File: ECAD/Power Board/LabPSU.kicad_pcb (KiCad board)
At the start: 2 copper layers, 83 parts, among them J1 CTRL, J2 DC-IN, J3 UPDI, J4 +, J5 -, Q1 Si7148DP, Q2 Si7148DP, U1 LM1117-3.3, U2 LM2594HVN-5.0, U3 LM5118MH, U4 TXB0104D, U5 LM358, U6 ATtiny414-SS, U7 INA180A3, U8 MCP4811

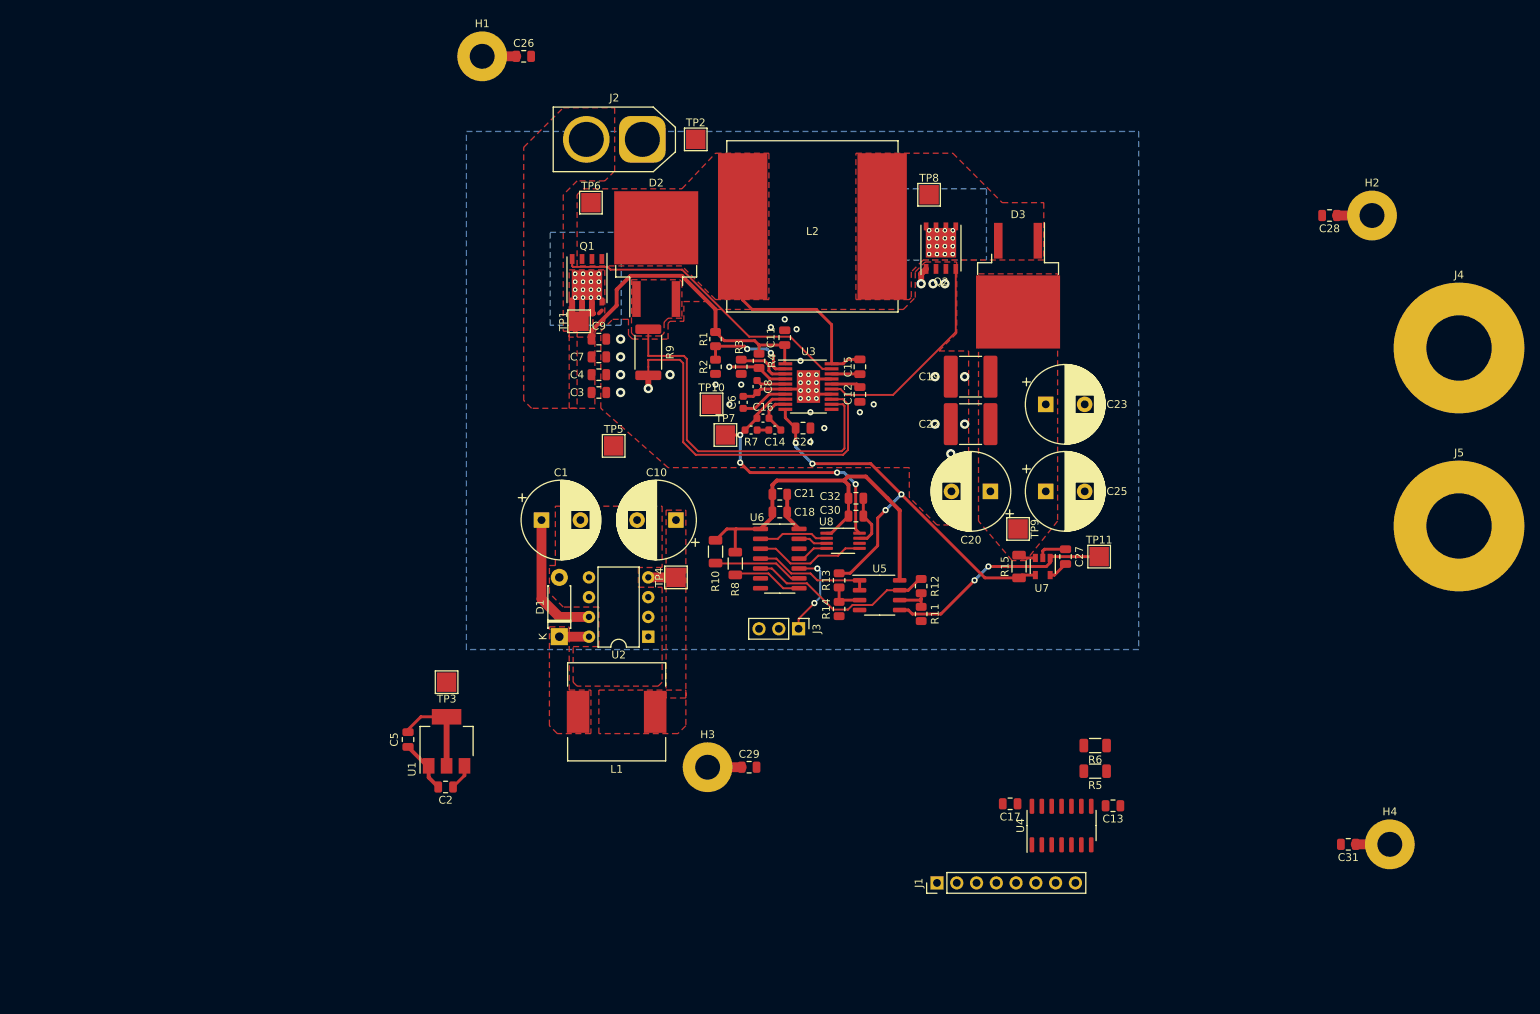
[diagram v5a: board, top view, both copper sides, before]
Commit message: Simplify the power board, remove level shifter
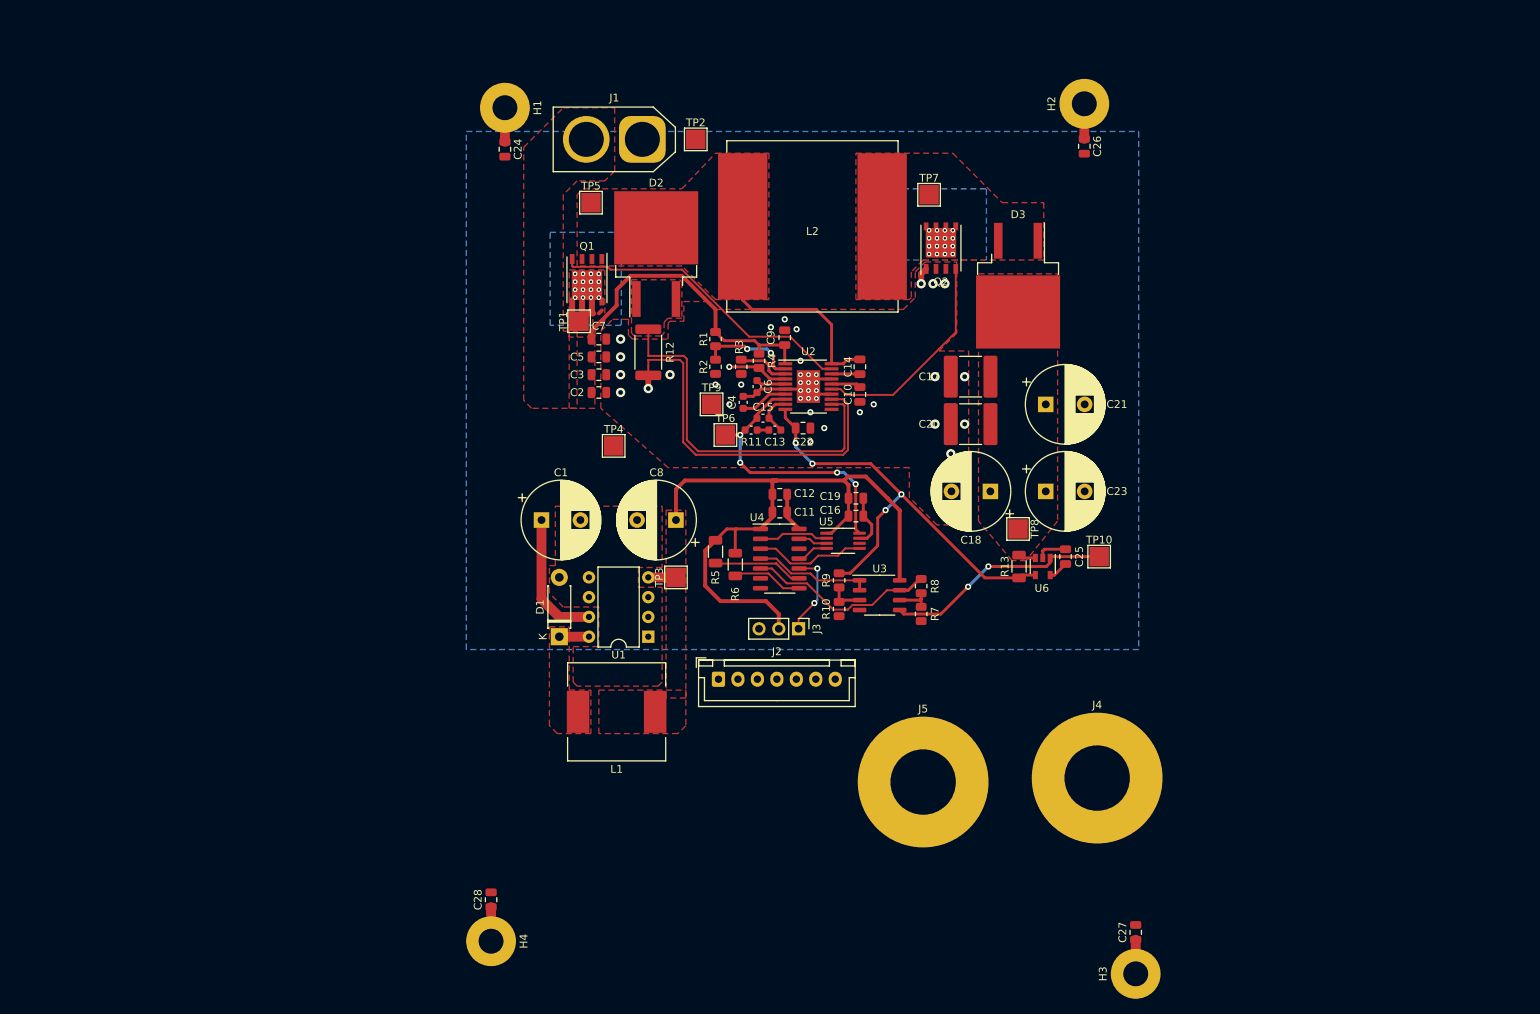
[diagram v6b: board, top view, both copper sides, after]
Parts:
- removed the C13 at (136.4, 146.8)
- removed the C17 at (123.2, 146.6)
- removed the C2 at (50.7, 144.4)
- removed the C5 at (45.8, 138.3)
- removed the J1 at (113.8, 156.7)
- removed the R5 at (134.1, 142.4)
- removed the R6 at (134.1, 139.1)
- removed the TP3 at (50.8, 130.9)
- removed the U1 at (50.8, 138.5)
- removed the U4 at (129.8, 149.4)
- added J2: CTRL, Connector_JST:JST_XH_B7B-XH-A_1x07_P2.50mm_Vertical, F.Cu at (85.7, 130.6)
- moved H4 116.1 mm to (56.5, 164.2), turned to 270 degrees
- moved C28 110.3 mm to (56.5, 158.9), turned to 90 degrees
- moved J5 76.3 mm to (112.0, 143.8)
- moved J4 72.2 mm to (134.4, 143.3)
- moved H3 61.1 mm to (139.3, 168.4), turned to 90 degrees
- moved C27 54.0 mm to (139.3, 163.1), turned to 90 degrees
- moved H2 39.6 mm to (132.7, 56.6), turned to 90 degrees
- moved C26 32.7 mm to (132.7, 62.1), turned to 270 degrees
- moved C24 12.2 mm to (58.3, 62.5), turned to 270 degrees
- moved H1 7.22 mm to (58.3, 57.1), turned to 270 degrees
- moved R6 3.03 mm to (87.9, 115.8)
- moved R5 2.96 mm to (85.3, 114.2)
- renumbered C12 to C10, C18 to C11, C21 to C12, C14 to C13, C15 to C14, C16 to C15, C30 to C16, C19 to C17, C20 to C18, C32 to C19, C3 to C2, C22 to C20, C23 to C21, C24 to C22, C25 to C23, C26 to C24, C27 to C25, C28 to C26, C29 to C27, C31 to C28, C4 to C3, C6 to C4, C7 to C5, C8 to C6, C9 to C7, C10 to C8, C11 to C9, J2 to J1, R14 to R10, R7 to R11, R9 to R12, R15 to R13, R8 to R5, R10 to R6, R11 to R7, R12 to R8, R13 to R9, TP11 to TP10, TP4 to TP3, TP5 to TP4, TP6 to TP5, TP7 to TP6, TP8 to TP7, TP9 to TP8, TP10 to TP9, U2 to U1, U3 to U2, U5 to U3, U6 to U4, U8 to U5, U7 to U6
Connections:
- R5 pad 2: SDA -> SCL
- R6 pad 2: SCL -> SDA
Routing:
- net +5V: track 61.4 -> 95.1 mm
- net +3V3: track 12.3 -> 0.00 mm
- net GND: track 43.6 -> 36.7 mm

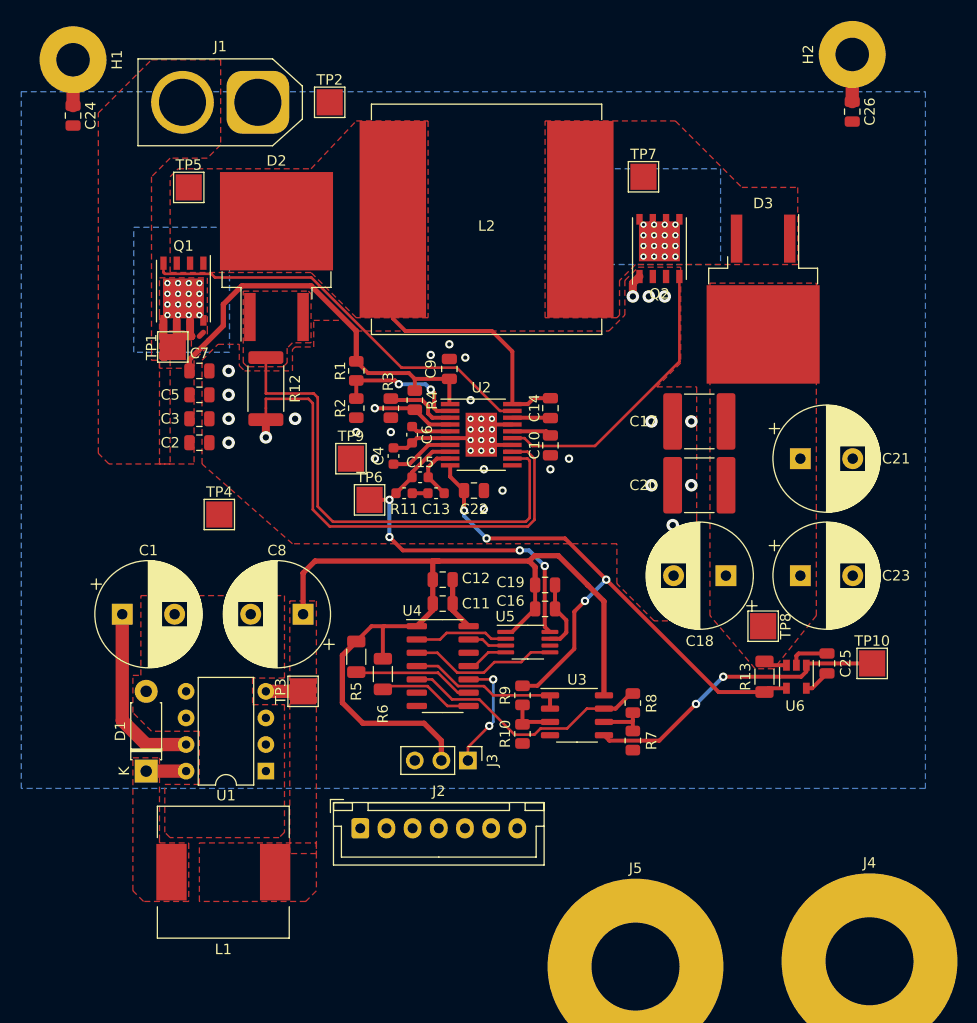
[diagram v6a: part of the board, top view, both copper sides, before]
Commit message: Place header
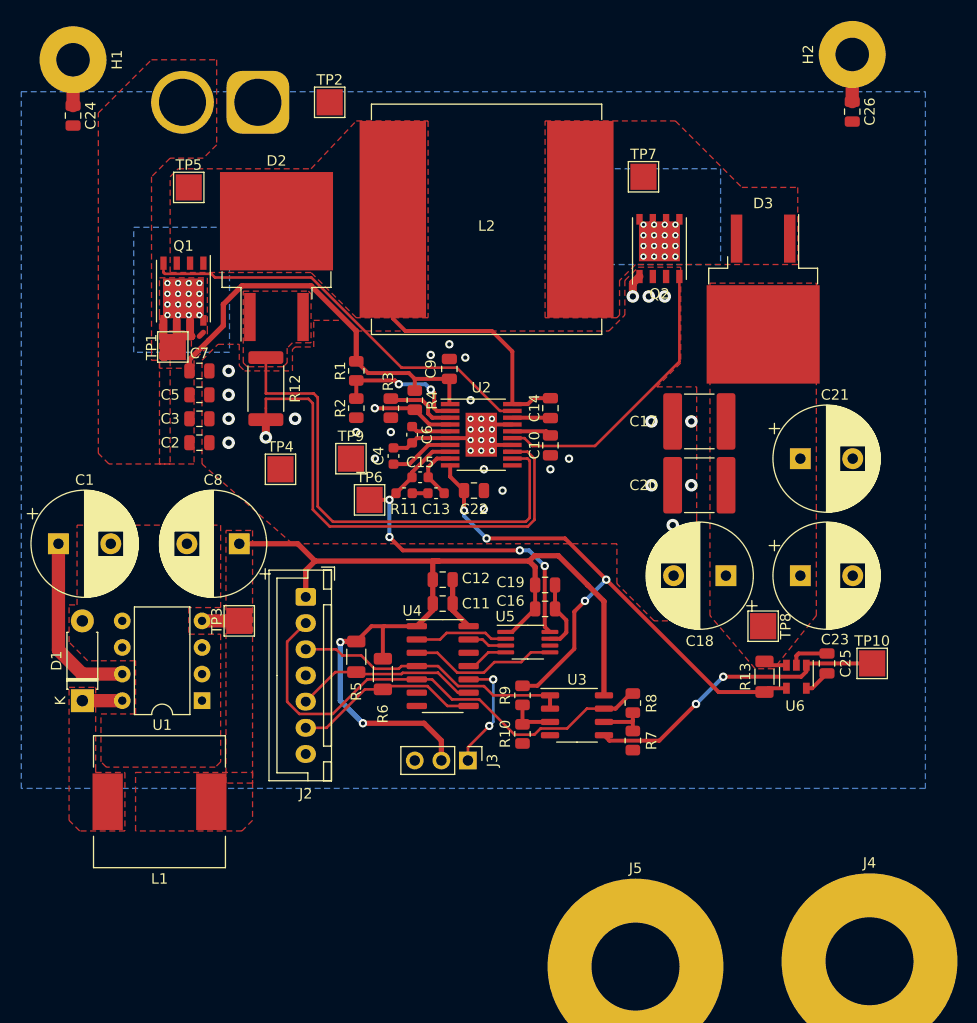
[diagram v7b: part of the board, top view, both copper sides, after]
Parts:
- J1: moved to B.Cu
- moved J2 22.7 mm to (80.5, 108.5), turned to 270 degrees
- moved L1 9.08 mm to (66.5, 128.0)
- moved D1 9.08 mm to (59.2, 118.4)
- moved U1 9.08 mm to (70.6, 118.4)
- moved C1 9.08 mm to (56.9, 103.4)
- moved C8 9.08 mm to (74.2, 103.4)
- moved TP3 9.08 mm to (74.2, 110.7)
- moved TP4 7.26 mm to (78.1, 96.3)
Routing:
- net IOUTBUF: track 24.5 -> 46.9 mm
- net VOUTBUF: track 15.2 -> 26.6 mm
- net SDA: track 9.10 -> 18.0 mm
- net +5V: track 95.1 -> 102.3 mm, vias 0 -> 2
- net SCL: track 11.6 -> 17.7 mm

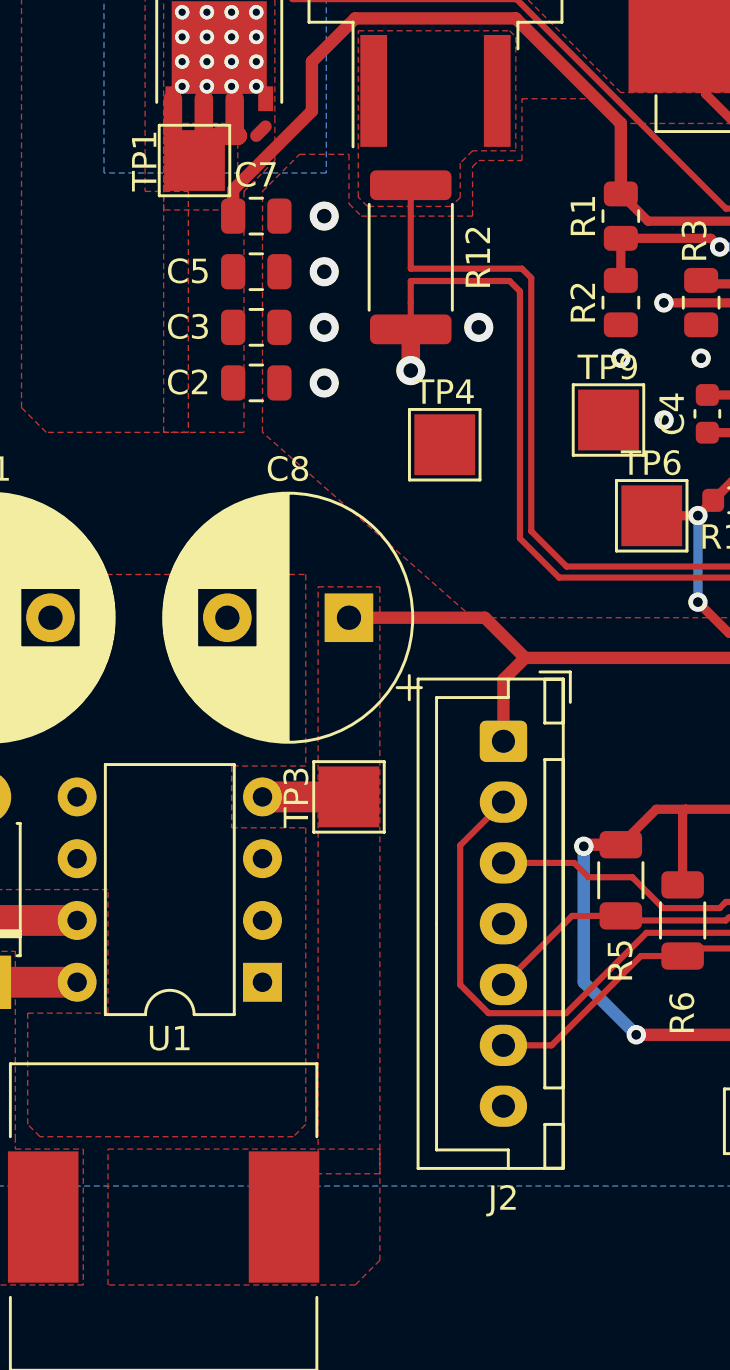
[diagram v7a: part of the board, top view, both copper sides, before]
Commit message: better component selection
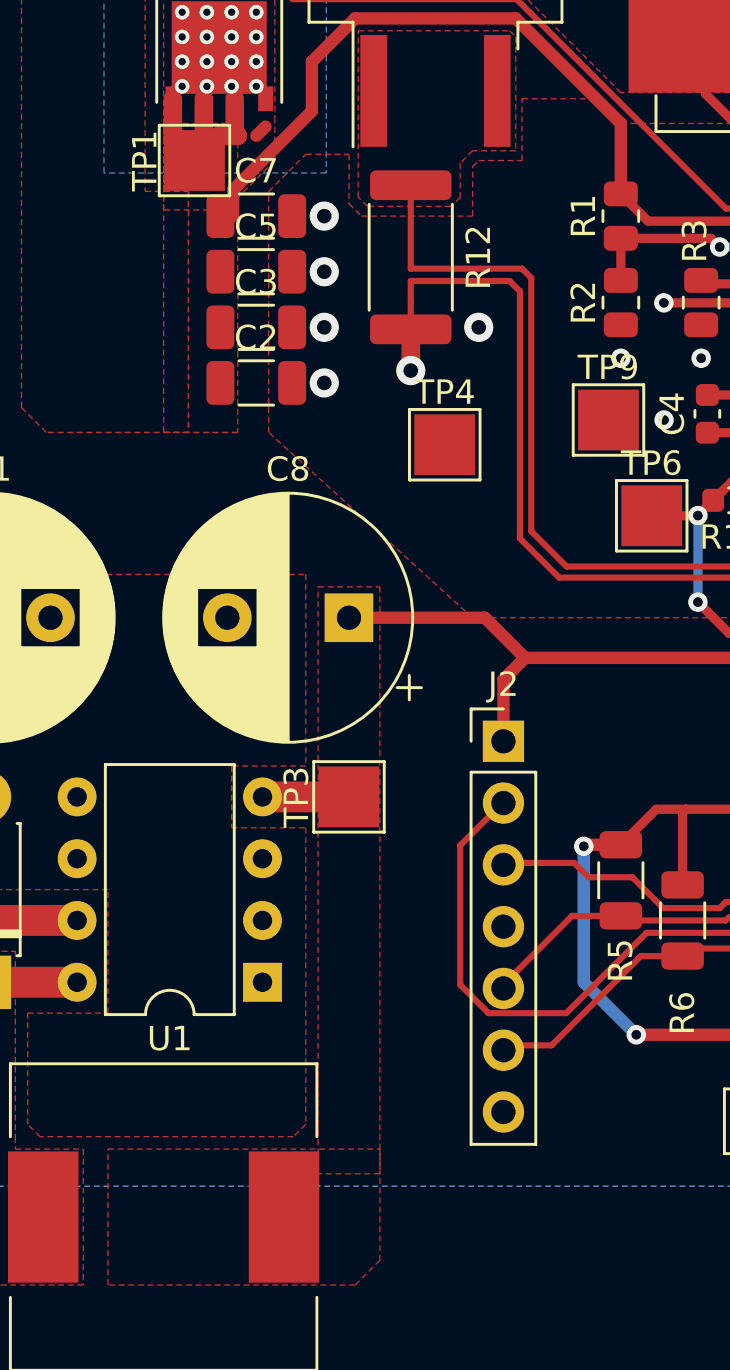
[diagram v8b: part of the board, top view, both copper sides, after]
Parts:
- C2, C3, C5, C7: footprint Capacitor_SMD:C_0805_2012Metric -> Capacitor_SMD:C_1206_3216Metric
- J2: footprint Connector_JST:JST_XH_B7B-XH-A_1x07_P2.50mm_Vertical -> Connector_PinHeader_2.54mm:PinHeader_1x07_P2.54mm_Vertical
- turned J2 to 0 degrees
